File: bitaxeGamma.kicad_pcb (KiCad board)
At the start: 4 copper layers, 56.5 x 99.8 mm, 146 parts, among them J1 54-00164, J2 TC2030-IDC, J3 Conn_01x04, J4 Conn_01x06, J5 USB_C_Receptacle_USB2.0, J6 Conn_01x04, J7 Conn_01x04, SW1 GT-TC029B-H025-L1N, SW2 GT-TC029B-H025-L1N, T1 net-tie, U10 EMC2101, U2 TPS546D24ARVFR, U3 RT9080-33GJ5, U4 ESP32-S3-WROOM-1, U5 MCP1824T-1202E/OT, U6 MCP1824T-0802E, U7 25MHz, U8 BM1370_mode1, U9 SN74AVC4T774

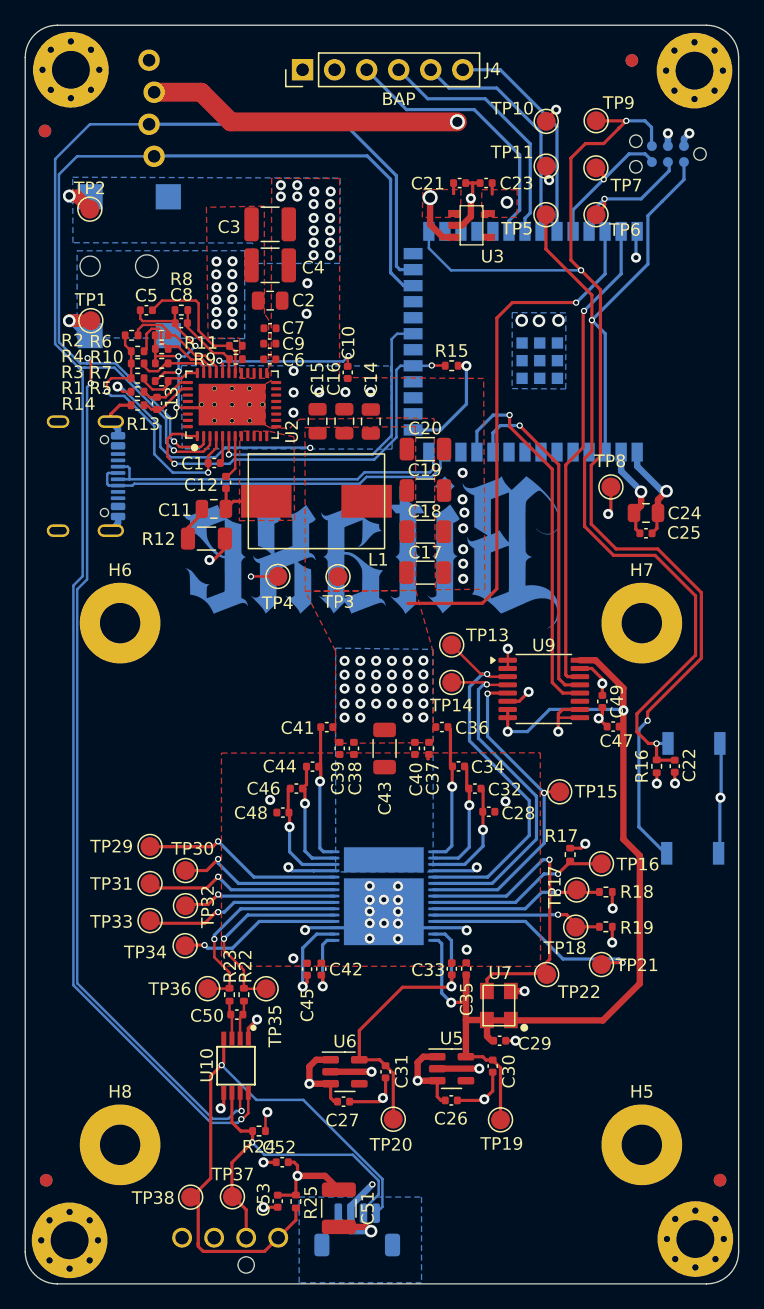
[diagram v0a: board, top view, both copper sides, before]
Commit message: Cleaned up zones, increased vdd trace width
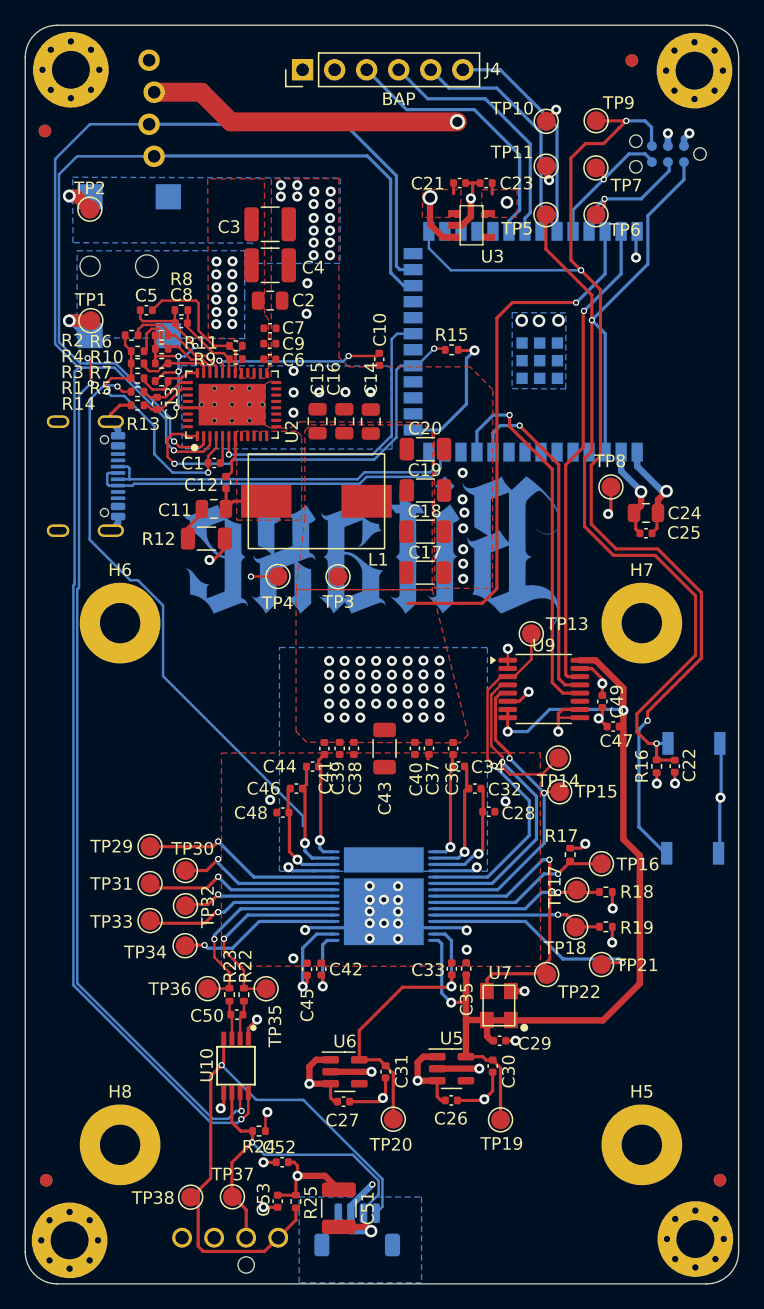
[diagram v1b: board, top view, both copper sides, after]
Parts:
- moved TP14 10.4 mm to (119.5, 105.6)
- moved TP13 6.37 mm to (117.3, 95.8)
- moved C10 2.71 mm to (105.2, 74.0)
- moved C36 1.92 mm to (111.1, 104.8), turned to 90 degrees
- moved C41 1.71 mm to (100.9, 104.8), turned to -90 degrees
- moved R15 1.26 mm to (111.0, 73.2)
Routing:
- net /VDD: track 62.6 -> 87.5 mm, vias 31 -> 40
- net /BM1370/VDD1_0: track 11.3 -> 8.94 mm
- net /3V3: track 54.8 -> 57.0 mm
- net /BM1370/VDD1_1: track 10.8 -> 8.74 mm
- net /BM1370/RST_N: track 30.1 -> 28.4 mm
- net Net-(U2-VDD5): track 12.4 -> 14.1 mm
- net /BM1370/CI: track 28.7 -> 30.2 mm
- net /BM1370/RO: track 27.0 -> 25.9 mm
- net /Power/PGOOD: track 32.6 -> 33.2 mm

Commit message: mounting holes to 3mm
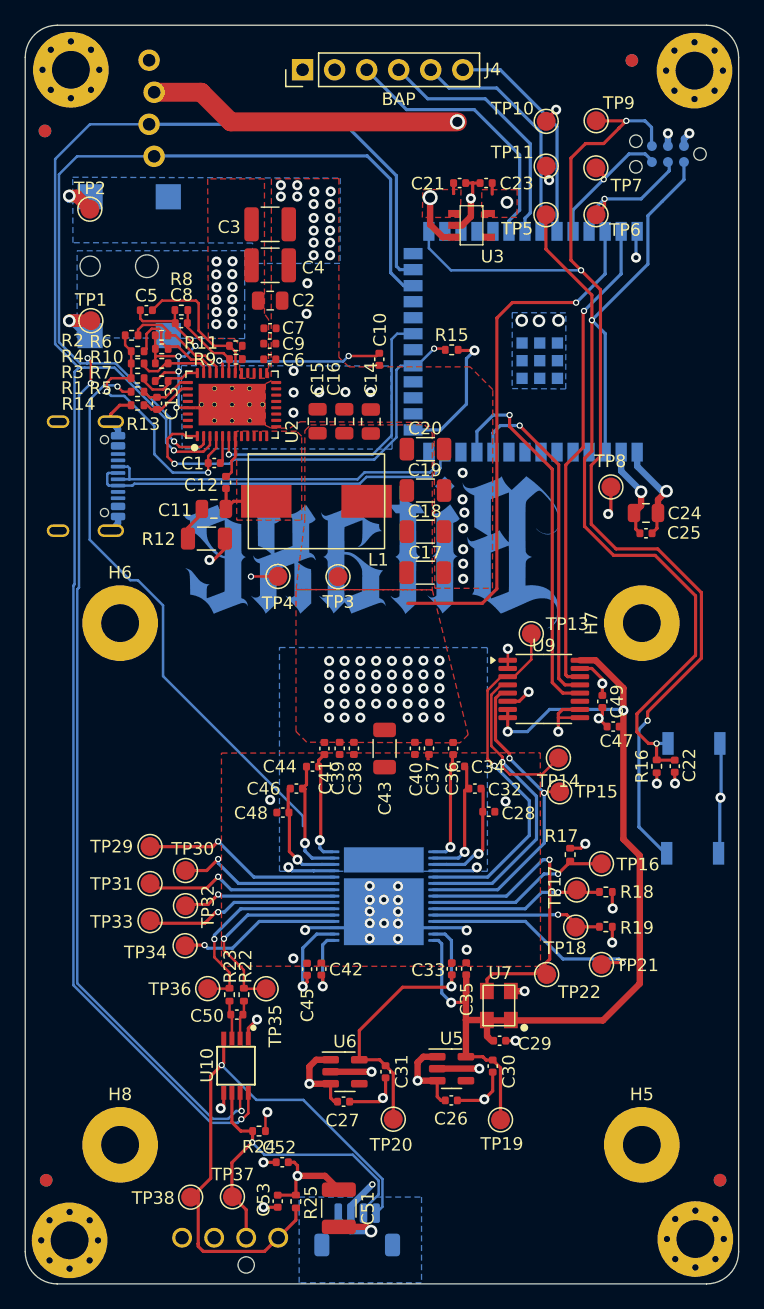
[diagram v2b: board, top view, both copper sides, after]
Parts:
- H5, H6, H7, H8: footprint MountingHole:MountingHole_3.2mm_M3_Pad -> MountingHole:MountingHole_3mm_Pad
- turned H7 to 90 degrees
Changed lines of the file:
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@@
 		)
 	)
-	(footprint "MountingHole:MountingHole_3.2mm_M3_Pad"
+	(footprint "MountingHole:MountingHole_3mm_Pad"
 		(layer "F.Cu")
 		(at 84.71 94.91)
-		(descr "Mounting Hole 3.2mm, M3")
-		(tags "mounting hole 3.2mm m3")
+		(descr "Mounting Hole 3mm")
+		(tags "mounting hole 3mm")
 		(property "Reference" "H6"
-			(at 0 -4.2 0)
+			(at 0 -4 0)
 			(layer "F.SilkS")
 			(effects
@@
 		)
 		(property "Value" "MountingHole"
-			(at 0 4.2 0)
+			(at 0 4 0)
 			(layer "F.Fab")
 			(effects
@@
 			)
 		)
-		(property "Footprint" "MountingHole:MountingHole_3.2mm_M3_Pad"
+		(property "Footprint" "MountingHole:MountingHole_3mm_Pad"
 			(at 0 0 0)
 			(unlocked yes)
@@
 		(sheetname "Root")
 		(sheetfile "bitaxeGamma.kicad_sch")
-		(zone_connect 2)
 		(attr exclude_from_pos_files exclude_from_bom)
 		(fp_circle
 			(center 0 0)
-			(end 3.2 0)
+			(end 3 0)
 			(stroke
 				(width 0.15)
@@
 		(fp_circle
 			(center 0 0)
-			(end 3.45 0)
+			(end 3.25 0)
 			(stroke
 				(width 0.05)
@@
 		(pad "1" thru_hole circle
 			(at 0 0)
-			(size 6.4 6.4)
-			(drill 3.2)
+			(size 6 6)
+			(drill 3)
 			(layers "*.Cu" "*.Mask")
 			(remove_unused_layers no)
@@
 		)
 	)
-	(footprint "MountingHole:MountingHole_3.2mm_M3_Pad"
+	(footprint "MountingHole:MountingHole_3mm_Pad"
 		(layer "F.Cu")
 		(at 126.06 136.26)
-		(descr "Mounting Hole 3.2mm, M3")
-		(tags "mounting hole 3.2mm m3")
+		(descr "Mounting Hole 3mm")
+		(tags "mounting hole 3mm")
 		(property "Reference" "H5"
-			(at 0 -4.2 0)
+			(at 0 -4 0)
 			(layer "F.SilkS")
 			(effects
@@
 		)
 		(property "Value" "MountingHole"
-			(at 0 4.2 0)
+			(at 0 4 0)
 			(layer "F.Fab")
 			(effects
@@
 			)
 		)
-		(property "Footprint" "MountingHole:MountingHole_3.2mm_M3_Pad"
+		(property "Footprint" "MountingHole:MountingHole_3mm_Pad"
 			(at 0 0 0)
 			(unlocked yes)
@@
 		(sheetname "Root")
 		(sheetfile "bitaxeGamma.kicad_sch")
-		(zone_connect 2)
 		(attr exclude_from_pos_files exclude_from_bom)
 		(fp_circle
 			(center 0 0)
-			(end 3.2 0)
+			(end 3 0)
 			(stroke
 				(width 0.15)
@@
 		(fp_circle
 			(center 0 0)
-			(end 3.45 0)
+			(end 3.25 0)
 			(stroke
 				(width 0.05)
@@
 		(pad "1" thru_hole circle
 			(at 0 0)
-			(size 6.4 6.4)
-			(drill 3.2)
+			(size 6 6)
+			(drill 3)
 			(layers "*.Cu" "*.Mask")
 			(remove_unused_layers no)
@@
 		)
 	)
-	(footprint "MountingHole:MountingHole_3.2mm_M3_Pad"
+	(footprint "MountingHole:MountingHole_3mm_Pad"
 		(layer "F.Cu")
 		(at 84.71 136.26)
-		(descr "Mounting Hole 3.2mm, M3")
-		(tags "mounting hole 3.2mm m3")
+		(descr "Mounting Hole 3mm")
+		(tags "mounting hole 3mm")
 		(property "Reference" "H8"
-			(at 0 -4.2 0)
+			(at 0 -4 0)
 			(layer "F.SilkS")
 			(effects
@@
 		)
 		(property "Value" "MountingHole"
-			(at 0 4.2 0)
+			(at 0 4 0)
 			(layer "F.Fab")
 			(effects
@@
 			)
 		)
-		(property "Footprint" "MountingHole:MountingHole_3.2mm_M3_Pad"
+		(property "Footprint" "MountingHole:MountingHole_3mm_Pad"
 			(at 0 0 0)
 			(unlocked yes)
@@
 		(sheetname "Root")
 		(sheetfile "bitaxeGamma.kicad_sch")
-		(zone_connect 2)
 		(attr exclude_from_pos_files exclude_from_bom)
 		(fp_circle
 			(center 0 0)
-			(end 3.2 0)
+			(end 3 0)
 			(stroke
 				(width 0.15)
@@
 		(fp_circle
 			(center 0 0)
-			(end 3.45 0)
+			(end 3.25 0)
 			(stroke
 				(width 0.05)
@@
 		(pad "1" thru_hole circle
 			(at 0 0)
-			(size 6.4 6.4)
-			(drill 3.2)
+			(size 6 6)
+			(drill 3)
 			(layers "*.Cu" "*.Mask")
 			(remove_unused_layers no)
@@
 		)
 	)
-	(footprint "MountingHole:MountingHole_3.2mm_M3_Pad"
+	(footprint "MountingHole:MountingHole_3mm_Pad"
 		(layer "F.Cu")
-		(at 126.06 94.91)
-		(descr "Mounting Hole 3.2mm, M3")
-		(tags "mounting hole 3.2mm m3")
+		(at 126.06 94.91 90)
+		(descr "Mounting Hole 3mm")
+		(tags "mounting hole 3mm")
 		(property "Reference" "H7"
-			(at 0 -4.2 0)
+			(at 0 -4 90)
 			(layer "F.SilkS")
 			(effects
@@
 		)
 		(property "Value" "MountingHole"
-			(at 0 4.2 0)
+			(at 0 4 90)
 			(layer "F.Fab")
 			(effects
@@
 			)
 		)
-		(property "Footprint" "MountingHole:MountingHole_3.2mm_M3_Pad"
-			(at 0 0 0)
+		(property "Footprint" "MountingHole:MountingHole_3mm_Pad"
+			(at 0 0 90)
 			(unlocked yes)
 			(layer "F.Fab")
@@
 		)
 		(property "Datasheet" ""
-			(at 0 0 0)
+			(at 0 0 90)
 			(unlocked yes)
 			(layer "F.Fab")
@@
 		)
 		(property "Description" "Mounting Hole with connection"
-			(at 0 0 0)
+			(at 0 0 90)
 			(unlocked yes)
 			(layer "F.Fab")
@@
 		(sheetname "Root")
 		(sheetfile "bitaxeGamma.kicad_sch")
-		(zone_connect 2)
 		(attr exclude_from_pos_files exclude_from_bom)
 		(fp_circle
 			(center 0 0)
-			(end 3.2 0)
+			(end 3 0)
 			(stroke
 				(width 0.15)
@@
 		(fp_circle
 			(center 0 0)
-			(end 3.45 0)
+			(end 3.25 0)
 			(stroke
 				(width 0.05)
@@
 		)
 		(fp_text user "${REFERENCE}"
-			(at 0 0 0)
+			(at 0 0 90)
 			(layer "F.Fab")
 			(effects
@@
 		)
 		(pad "1" thru_hole circle
-			(at 0 0)
-			(size 6.4 6.4)
-			(drill 3.2)
+			(at 0 0 90)
+			(size 6 6)
+			(drill 3)
 			(layers "*.Cu" "*.Mask")
 			(remove_unused_layers no)

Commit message: lots of misc
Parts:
- removed C14, C15, C16: 22uF, Capacitor_SMD:C_0805_2012Metric
- removed C25, C37, C38: 0.1uF, Capacitor_SMD:C_0402_1005Metric
- removed C39, C40, C7: 1uF, Capacitor_SMD:C_0402_1005Metric
- removed C6: 4700pF, Capacitor_SMD:C_0402_1005Metric
- removed C9: 2200pF, Capacitor_SMD:C_0402_1005Metric
- removed R2, R3, R4, R7: ~, Resistor_SMD:R_0402_1005Metric
- added C54: 100uF, Capacitor_SMD:C_1206_3216Metric, F.Cu at (106.9, 108.5)
- C2: value 10uF -> 100uF; footprint Capacitor_SMD:C_0805_2012Metric -> Capacitor_SMD:C_1206_3216Metric
- C3, C4, C51: value 47uF -> 100uF; footprint Capacitor_SMD:C_1210_3225Metric -> Capacitor_SMD:C_1206_3216Metric
- TP10, TP11, TP5, TP6, TP7, TP9: footprint TestPoint:TestPoint_Pad_D1.5mm -> TestPoint:TestPoint_Pad_D2.5mm
- moved C2 12.2 mm to (104.7, 78.6), turned to 90 degrees
- moved C3 7.68 mm to (97.2, 71.0)
- moved C4 6.88 mm to (97.2, 73.4)
- moved C51 4.75 mm to (102.8, 136.6)
- moved C34 4.11 mm to (111.5, 110.4)
- moved C44 4.09 mm to (99.8, 110.4)
- moved C43 3.89 mm to (104.3, 108.5)
- moved C53 3.81 mm to (99.3, 137.6)
- moved TP8 3.80 mm to (124.5, 87.8)
- moved R25 3.65 mm to (100.4, 137.6)
- moved C41 3.56 mm to (100.6, 108.4)
- moved C36 3.56 mm to (110.8, 108.4)
- moved C32 3.41 mm to (112.5, 111.4)
- moved C46 3.33 mm to (98.8, 111.3)
- moved C52 3.03 mm to (99.5, 135.3)
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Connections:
- C2 pad 1: /5V -> /VDD
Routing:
- net /Power/AGND: track 20.1 -> 13.4 mm, vias 4 -> 3
- net GND: track 97.0 -> 90.8 mm, vias 81 -> 110
- net Net-(U2-ADRSEL): track 6.01 -> 0.00 mm
- net Net-(U2-VSEL): track 8.95 -> 3.88 mm
- net Net-(U2-AVIN): track 11.5 -> 7.05 mm
- net /BM1370/VDD2_0: track 9.57 -> 5.38 mm
- net /BM1370/VDD2_1: track 9.40 -> 5.27 mm
- net Net-(U2-MSEL2): track 8.87 -> 4.81 mm
- net /Fan/FAN_PWM: track 46.8 -> 50.7 mm
- net Net-(U2-BP1V5): track 21.5 -> 17.9 mm
- net /BM1370/VDD3_0: track 9.36 -> 5.83 mm
- net /3V3: track 57.0 -> 53.5 mm
- net /BM1370/VDD1_1: track 8.74 -> 5.30 mm
- net /BM1370/VDD3_1: track 9.02 -> 5.61 mm
- net /BM1370/VDD1_0: track 8.94 -> 5.73 mm
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- added copper zone on In2.Cu, net /Power/SW
- added copper zone on In2.Cu, net /VDD

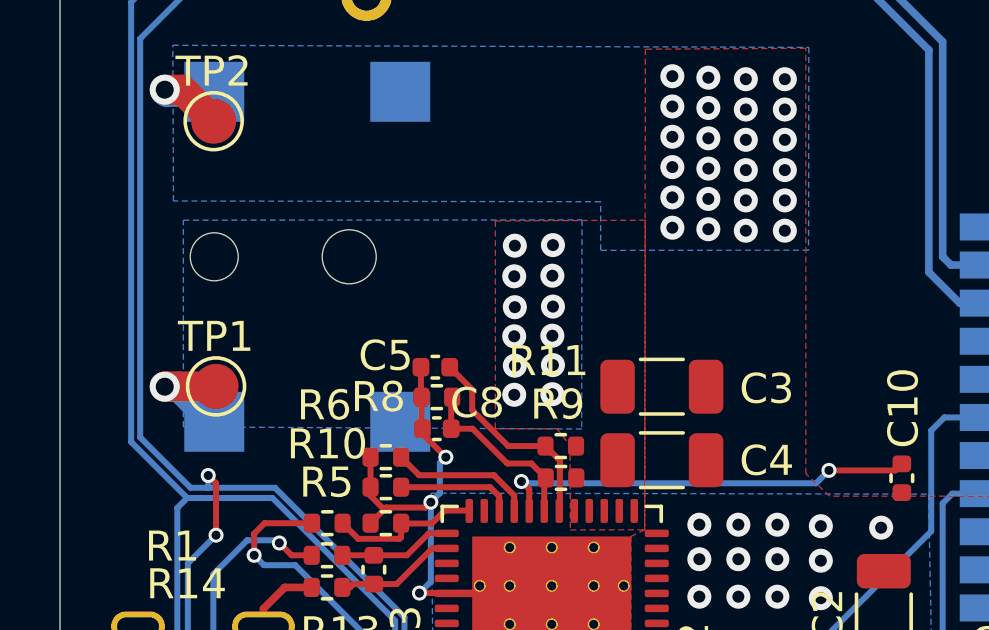
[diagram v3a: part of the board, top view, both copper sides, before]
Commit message: more input vias
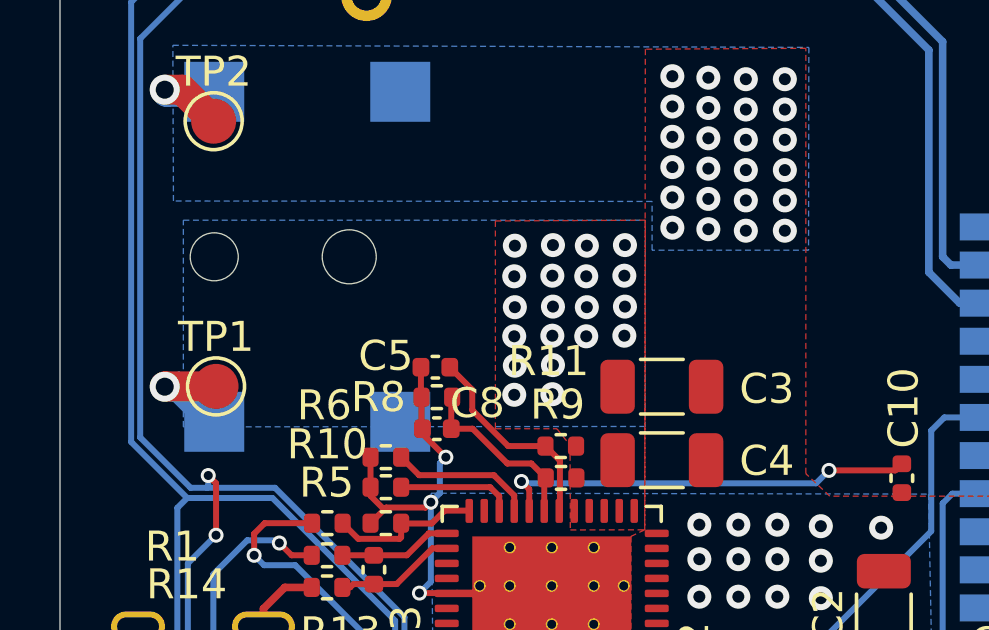
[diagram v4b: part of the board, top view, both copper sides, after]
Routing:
- net /5V: vias 18 -> 26
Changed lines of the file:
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@@
 	)
 	(via
+		(at 94.75 68.3)
+		(size 0.8)
+		(drill 0.4)
+		(layers "F.Cu" "B.Cu")
+		(free yes)
+		(net 4)
+	)
+	(via
 		(at 92.35 66.25)
 		(size 0.8)
@@
 	)
 	(via
+		(at 96.02 66.23)
+		(size 0.8)
+		(drill 0.4)
+		(layers "F.Cu" "B.Cu")
+		(free yes)
+		(net 4)
+	)
+	(via
 		(at 109.28 61.185155)
 		(size 1.2)
@@
 	)
 	(via
+		(at 96 67.25)
+		(size 0.8)
+		(drill 0.4)
+		(layers "F.Cu" "B.Cu")
+		(free yes)
+		(net 4)
+	)
+	(via
+		(at 94.73 67.27)
+		(size 0.8)
+		(drill 0.4)
+		(layers "F.Cu" "B.Cu")
+		(free yes)
+		(net 4)
+	)
+	(via
+		(at 94.75 66.25)
+		(size 0.8)
+		(drill 0.4)
+		(layers "F.Cu" "B.Cu")
+		(free yes)
+		(net 4)
+	)
+	(via
 		(at 80.68 70.95)
 		(size 1)
@@
 	)
 	(via
+		(at 96.02 68.28)
+		(size 0.8)
+		(drill 0.4)
+		(layers "F.Cu" "B.Cu")
+		(free yes)
+		(net 4)
+	)
+	(via
 		(at 92.33 69.27)
 		(size 0.8)
@@
 		(net 4)
 	)
+	(via
+		(at 96 69.25)
+		(size 0.8)
+		(drill 0.4)
+		(layers "F.Cu" "B.Cu")
+		(free yes)
+		(net 4)
+	)
+	(via
+		(at 94.73 69.27)
+		(size 0.8)
+		(drill 0.4)
+		(layers "F.Cu" "B.Cu")
+		(free yes)
+		(net 4)
+	)
 	(segment
 		(start 92.3224 55.3176)
@@
 		(polygon
 			(pts
-				(xy 81.3 65.4) (xy 94.59 65.39) (xy 94.58 68.9) (xy 94.58 72.36) (xy 81.3 72.29)
+				(xy 81.3 65.4) (xy 96.7 65.4) (xy 96.7 72.275) (xy 81.3 72.29)
 			)
 		)
@@
 		(polygon
 			(pts
-				(xy 80.95 59.57) (xy 102.15 59.64) (xy 102.14 66.4) (xy 95.21 66.405061) (xy 95.21 64.784722) (xy 80.97 64.76)
+				(xy 80.95 59.57) (xy 102.15 59.64) (xy 102.14 66.4) (xy 96.925 66.4) (xy 96.925 64.775) (xy 80.97 64.76)
 			)
 		)
